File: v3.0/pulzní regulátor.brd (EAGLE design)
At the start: 163.9 x 100.6 mm, 24 parts, among them Q1 BS170, Q2 BS170, Q3 BS170, Q4 BS170

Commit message: přidání řízení DAC1 a ADC
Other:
- board size 163.9 x 100.6 mm -> 63.6 x 42.2 mm
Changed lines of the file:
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@@
 <fusionsync huburn="a.YnVzaW5lc3M6c3BzdHJ1dG5vdjM" projecturn="a.YnVzaW5lc3M6c3BzdHJ1dG5vdjMjMjAyMDAzMzEyODExMTAyMDY" f3durn="urn:adsk.wipprod:dm.lineage:tzPS94EqTMquKnj5MIRSqw" pcbguid="5c4cd1a3-4ed4-4477-aad7-c409a0e1ec90" lastpulledtime="" lastsyncedchangeguid="bf5b5c15-012f-dc76-c788-9961873cef67"/>
 <plain>
-<wire x1="-3.937" y1="-0.635" x2="159.873" y2="-0.635" width="0" layer="20"/>
-<wire x1="159.873" y1="-0.635" x2="160" y2="100" width="0" layer="20"/>
-<wire x1="160" y1="100" x2="-3.81" y2="98.73" width="0" layer="20"/>
-<wire x1="-3.81" y1="98.73" x2="-3.937" y2="-0.635" width="0" layer="20"/>
+<wire x1="-3.937" y1="-0.635" x2="59.543" y2="-0.635" width="0" layer="20"/>
+<wire x1="59.543" y1="-0.635" x2="59.67" y2="41.58" width="0" layer="20"/>
+<wire x1="59.67" y1="41.58" x2="-3.81" y2="41.58" width="0" layer="20"/>
+<wire x1="-3.81" y1="41.58" x2="-3.937" y2="-0.635" width="0" layer="20"/>
+<dimension x1="-3.81" y1="41.58" x2="-3.937" y2="-0.635" x3="-8.85893125" y3="20.487496875" textsize="1.778" layer="1"/>
+<dimension x1="59.67" y1="41.58" x2="-3.81" y2="41.58" x3="27.93" y3="46.99" textsize="1.778" layer="1"/>
 </plain>
 <attributes>

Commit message: opravena chyba pozice kurzoru v menu 1, změněn clock na externí, include knihoven eaglu.
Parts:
- R1: value (none) -> 1K5
- R2: value (none) -> 4K3
- R3: value (none) -> 5K1
- R4: value (none) -> 6K8
- R5: value (none) -> 15K
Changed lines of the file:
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@@
 <attribute name="VALUE" x="47.625" y="4.445" size="1.27" layer="27" ratio="10" rot="R270"/>
 </element>
-<element name="R1" library="rcl_my" package="M0805" value="" x="41.91" y="29.21" smashed="yes" rot="MR90">
+<element name="R1" library="rcl_my" package="M0805" value="1K5" x="41.91" y="29.21" smashed="yes" rot="MR90">
 <attribute name="NAME" x="43.18" y="27.94" size="1.27" layer="26" rot="MR90"/>
 <attribute name="VALUE" x="39.37" y="27.94" size="1.27" layer="28" rot="MR90"/>
 </element>
-<element name="R2" library="rcl_my" package="M0805" value="" x="44.45" y="29.21" smashed="yes" rot="MR90">
+<element name="R2" library="rcl_my" package="M0805" value="4K3" x="44.45" y="29.21" smashed="yes" rot="MR90">
 <attribute name="NAME" x="45.72" y="27.94" size="1.27" layer="26" rot="MR90"/>
 <attribute name="VALUE" x="41.91" y="27.94" size="1.27" layer="28" rot="MR90"/>
 </element>
-<element name="R3" library="rcl_my" package="M0805" value="" x="46.99" y="29.21" smashed="yes" rot="MR90">
+<element name="R3" library="rcl_my" package="M0805" value="5K1" x="46.99" y="29.21" smashed="yes" rot="MR90">
 <attribute name="NAME" x="48.26" y="27.94" size="1.27" layer="26" rot="MR90"/>
 <attribute name="VALUE" x="44.45" y="27.94" size="1.27" layer="28" rot="MR90"/>
 </element>
-<element name="R4" library="rcl_my" package="M0805" value="" x="49.53" y="29.21" smashed="yes" rot="MR90">
+<element name="R4" library="rcl_my" package="M0805" value="6K8" x="49.53" y="29.21" smashed="yes" rot="MR90">
 <attribute name="NAME" x="50.8" y="27.94" size="1.27" layer="26" rot="MR90"/>
 <attribute name="VALUE" x="46.99" y="27.94" size="1.27" layer="28" rot="MR90"/>
 </element>
-<element name="R5" library="rcl_my" package="M0805" value="" x="39.37" y="29.21" smashed="yes" rot="MR270">
+<element name="R5" library="rcl_my" package="M0805" value="15K" x="39.37" y="29.21" smashed="yes" rot="MR270">
 <attribute name="NAME" x="38.1" y="30.48" size="1.27" layer="26" rot="MR270"/>
 <attribute name="VALUE" x="41.91" y="30.48" size="1.27" layer="28" rot="MR270"/>

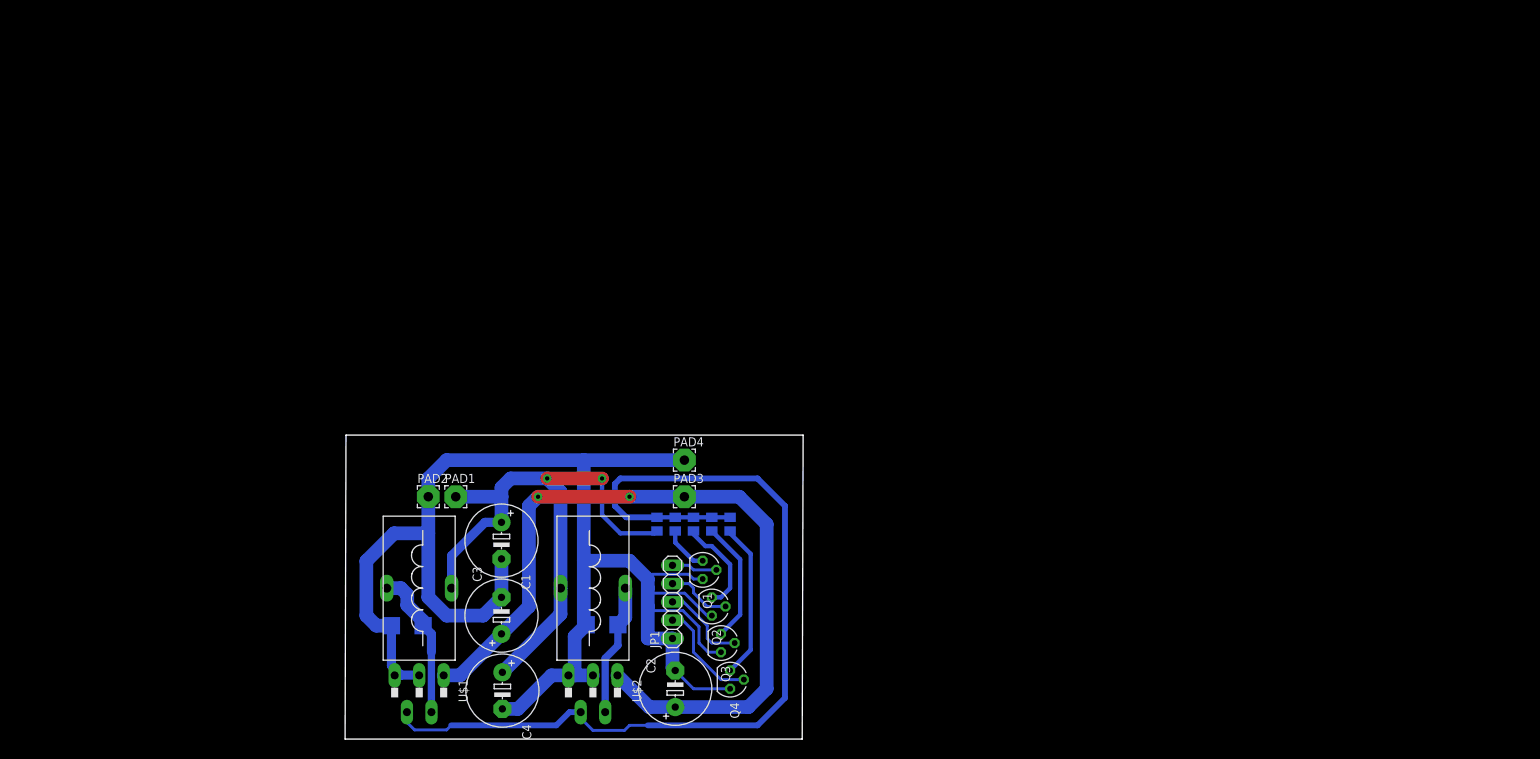
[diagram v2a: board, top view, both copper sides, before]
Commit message: Úprava BUCK regulátoru z 6A na 3A, osnova dokumentace
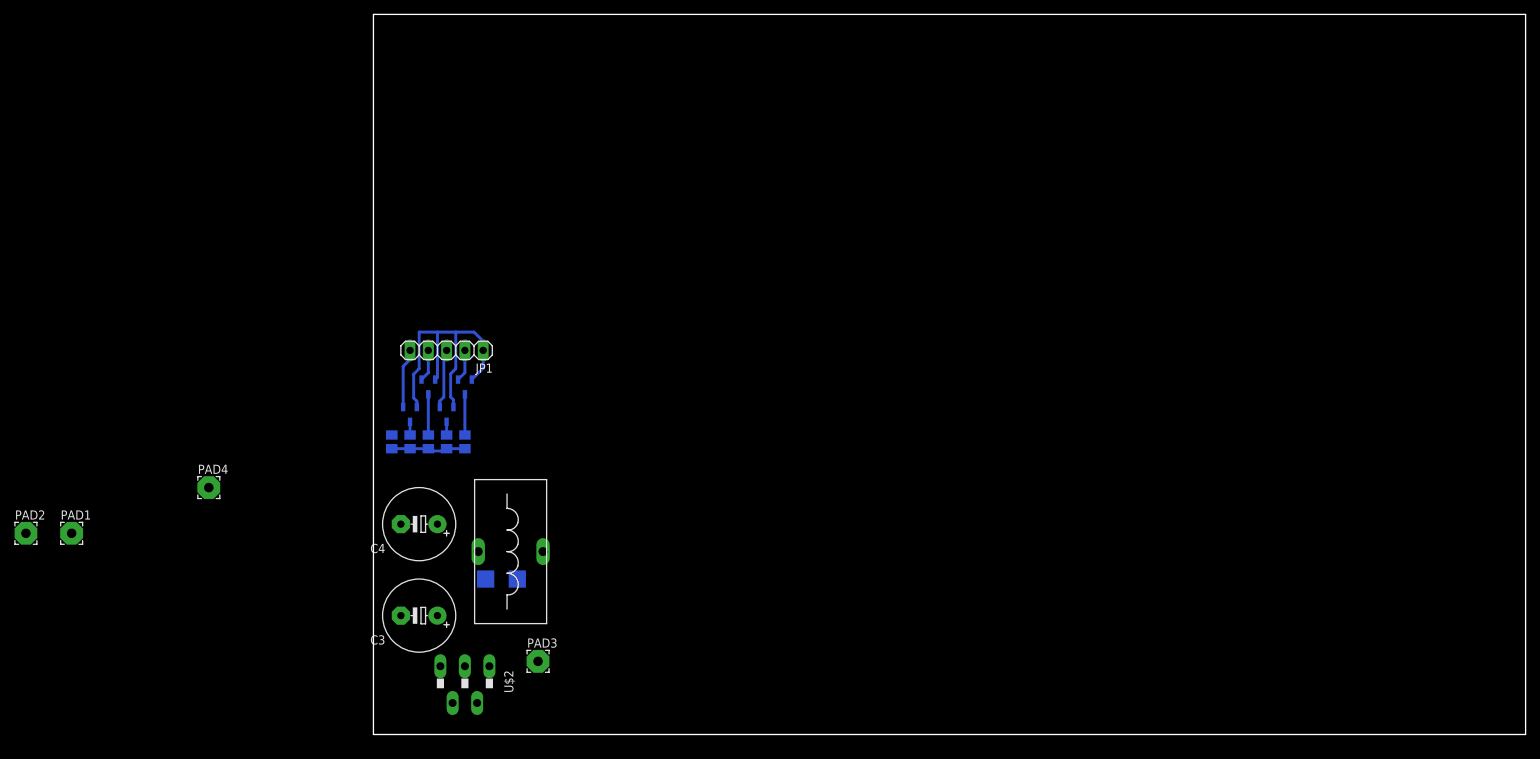
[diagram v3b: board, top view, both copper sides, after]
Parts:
- removed C1, C2: (no value), rcl:E5-10,5
- removed D1: MBRS130LT3, diode:SMB
- removed U$1: AP1501TO220, regulators:TO220-5
- removed U$3: DTMSSDTMSS-16/0,033/6,0, induktory a trafa:DTMSS-16/0,033/6,0
- Q1, Q2, Q3, Q4: value BS170 -> NX3008; device transistor-small-signal:SOT54E -> NEXPERIA :SOT95P240X110-3N
- moved PAD4 66.1 mm to (-22.9, 34.3)
- moved PAD2 56.1 mm to (-48.3, 27.9)
- moved Q4 54.8 mm to (12.7, 48.3), flipped to the bottom
- moved PAD1 53.6 mm to (-41.9, 27.9)
- moved Q2 49.8 mm to (7.62, 48.3), flipped to the bottom
- moved Q3 49.6 mm to (10.2, 44.5), flipped to the bottom
- moved JP1 46.9 mm to (10.2, 53.3), turned to 180 degrees
- moved Q1 46.0 mm to (5.08, 44.5), flipped to the bottom
- moved R2 38.6 mm to (7.62, 40.6), turned to 270 degrees
- moved R1 38.6 mm to (5.08, 40.6), turned to 270 degrees
- moved R3 38.6 mm to (10.2, 40.6), turned to 270 degrees
- moved R4 38.6 mm to (12.7, 40.6), turned to 270 degrees
- moved R5 38.6 mm to (2.54, 40.6), turned to 90 degrees
- moved PAD3 30.6 mm to (22.9, 10.2)
- moved C4 25.8 mm to (6.35, 29.2), turned to 180 degrees
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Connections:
- removed net N$2: D1.C, U$1.2, U$3.P$1
- net +24V: no longer C2.+, U$1.1
- net GND: now also Q1.2, Q2.2, Q3.2, Q4.2; no longer C1.-, C2.-, D1.A, Q1.S, Q2.S, Q3.S, Q4.S, U$1.3, U$1.5
- net N$1: now also Q4.3; no longer Q4.D
- net N$10: now also Q1.1; no longer Q1.G
- net N$11: now also Q2.3; no longer Q2.D
- net N$12: now also Q3.3; no longer Q3.D
- net N$5: now also Q4.1; no longer Q4.G
- net N$6: no longer U$1.4
- net N$7: now also Q1.3; no longer Q1.D
- net N$8: now also Q3.1; no longer Q3.G
- net N$9: now also Q2.1; no longer Q2.G
- net VCC: no longer C1.+, U$3.P$2
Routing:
- net GND: track 216.3 -> 43.9 mm
- net N$6: track 130.7 -> 10.9 mm
- net +24V: track 111.4 -> 0.00 mm, vias 2 -> 0
- net VCC: track 83.9 -> 0.00 mm, vias 2 -> 0
- net N$2: track 20.9 -> 0.00 mm
- net N$3: track 18.4 -> 0.00 mm
- net N$1: track 21.7 -> 5.65 mm
- net N$12: track 17.0 -> 1.84 mm
- net N$5: track 15.0 -> 4.45 mm
- net N$11: track 13.6 -> 5.65 mm
- net N$7: track 6.58 -> 1.84 mm
- net N$9: track 9.05 -> 4.45 mm
- net N$8: track 12.0 -> 8.35 mm
- net N$10: track 6.36 -> 8.26 mm
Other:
- board size 63.6 x 42.2 mm -> 160 x 100 mm

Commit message: regulováný zdroj pro 3A kompletní + dokumentace ovládacího panelu
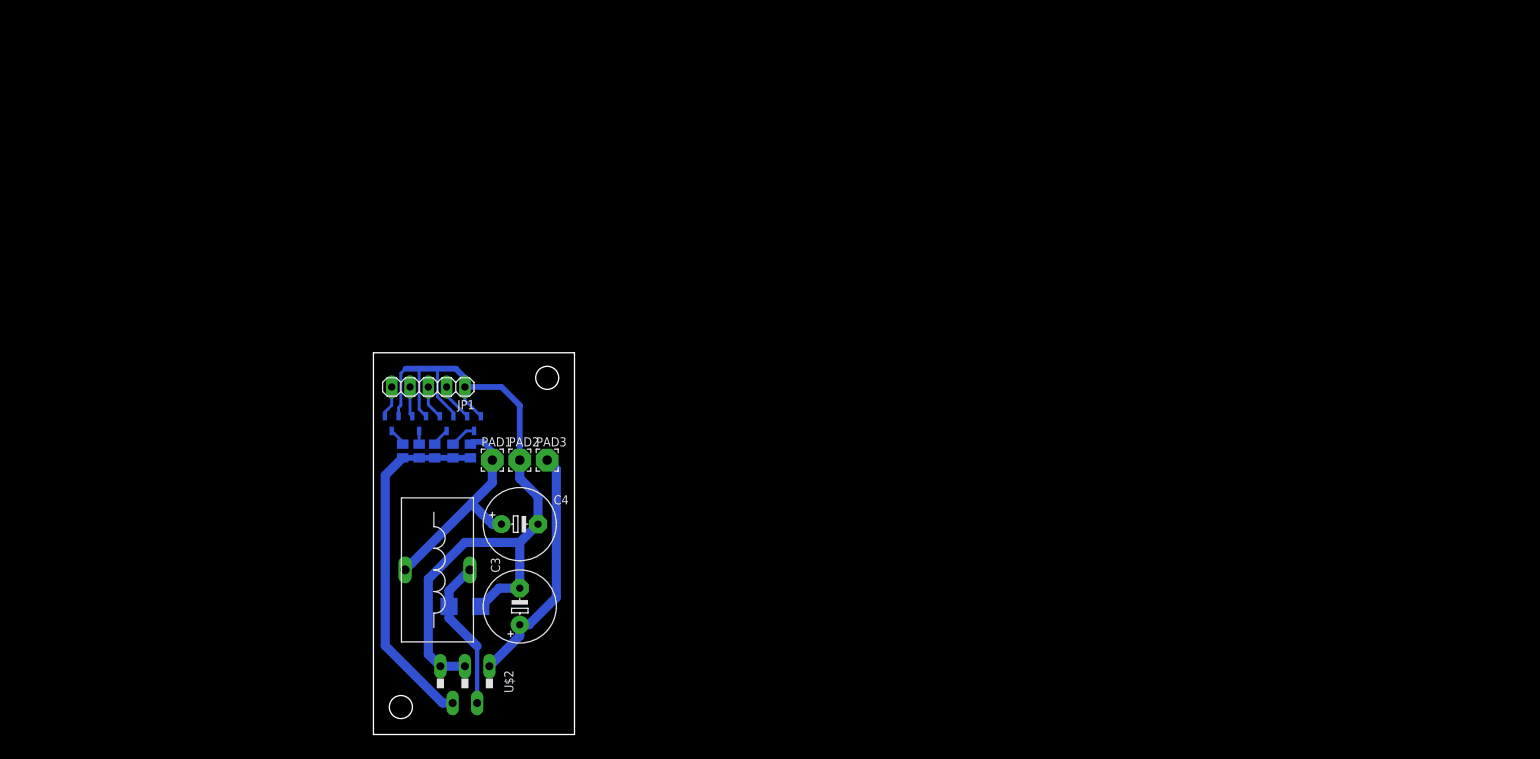
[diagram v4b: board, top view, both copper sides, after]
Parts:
- removed PAD4: (no value), wirepad:3,17/1,3
- moved PAD2 69.3 mm to (20.3, 38.1)
- moved PAD1 59.3 mm to (16.5, 38.1)
- moved PAD3 28.0 mm to (24.1, 38.1)
- moved C3 14.0 mm to (20.3, 17.8), turned to 90 degrees
- moved C4 14.0 mm to (20.3, 29.2), turned to 0 degrees
- moved R5 11.0 mm to (13.5, 39.4)
- moved U$4 10.5 mm to (8.89, 22.9)
- moved D2 6.35 mm to (12.7, 17.8), turned to 180 degrees
- moved JP1 5.68 mm to (7.62, 48.3)
- moved Q2 5.24 mm to (6.35, 43.2)
- moved Q4 5.24 mm to (14.0, 43.2)
- moved Q1 2.84 mm to (2.54, 43.2)
- moved R3 2.08 mm to (8.51, 39.4)
- moved R4 2.08 mm to (11.0, 39.4)
- moved R2 1.80 mm to (6.35, 39.4)
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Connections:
- net GND: no longer PAD4.1
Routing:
- net GND: track 43.9 -> 110.2 mm
- net N$6: track 10.9 -> 49.1 mm
- net +24V: track 0.00 -> 33.7 mm
- net VCC: track 0.00 -> 30.6 mm
- net N$3: track 0.00 -> 21.3 mm
- net N$10: track 8.26 -> 4.45 mm
- net N$11: track 5.65 -> 1.84 mm
- net N$8: track 8.35 -> 4.71 mm
- net N$1: track 5.65 -> 3.68 mm
- net N$5: track 4.45 -> 5.24 mm
- net N$12: track 1.84 -> 2.52 mm
- net N$7: track 1.84 -> 2.47 mm
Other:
- board size 160 x 100 mm -> 27.9 x 53 mm
